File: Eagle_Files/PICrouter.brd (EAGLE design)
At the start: 101.8 x 34 mm, 81 parts, among them IC1 PIC32MX675F512H, IC2 48M033F, IC3 DP83848, J3 POWER_JACK, Q1 20MHz, U1 DEVICE, X1 USB-A-H

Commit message: Released PICrouter schematic and board v0.91.
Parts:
- removed C25: 150uF, rcl:PANASONIC_C
- removed C27: 0.1uF, rcl:C2012
- removed D1, D2: (no value), diode:SOD123
- removed F1: PTCSMD, SparkFun:PTC-1206
- removed J3: POWER_JACK, SparkFun:POWER_JACK_PTH_LOCK
- removed Q2: (no value), transistor-small-signal:SOT23
- removed R7: 33k, SparkFun:0603-RES
- removed U1: DEVICE, SparkFun:USB-B-PTH
- removed X1: USB-A-H, SparkFun:USB-A-H
- added C28, C29, C31, C32: 0.1uF, rcl:C2012
- added C30: 10uF, rcl:C2012
- added F2: PTCSMD, SparkFun:PTC-1206
- added IC4: TPS2111A, SparkFun:TSSOP8
- added J1: POWER_JACK, SparkFun:POWER_JACK_PTH_LOCK
- added R28: 400, SparkFun:0603-RES
- added U2: DEVICE, SparkFun:USB-B-PTH
- added X2: USB-A-H, SparkFun:USB-A-H
- C10: value 0.1uF -> 150uF; device rcl:C2012 -> rcl:PANASONIC_C
- C13: value 10uF -> 150uF; device rcl:C2012 -> rcl:PANASONIC_C
- R6: value 100k -> 10k
- moved C13 21.2 mm to (-9.02, 3.81), turned to 0 degrees
- moved R5 13.2 mm to (31.2, 6.81), turned to 180 degrees
- moved C10 5.41 mm to (12.2, 8.89)
- moved R6 1.18 mm to (21.8, 11.7), turned to 270 degrees
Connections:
- removed net N$45: IC1.36, U1.D-, X1.D-
- removed net N$46: C10.1, C27.1, D1.A, J3.PWR, PW.1, Q2.1, R5.2, R7.2
- removed net N$5: IC1.37, U1.D+, X1.D+
- removed net N$50: C13.1, C25.+, C9.2, F1.1, IC1.34, Q2.2, R4.1, R6.2, U1.VBUS, X1.VBUS
- removed net N$60: D2.A, Q2.3
- new net D+: IC1.37, U2.D+, X2.D+
- new net D-: IC1.36, U2.D-, X2.D-
- new net N$61: IC4.4, R28.2
- new net SELF: C29.1, C31.1, C32.1, IC4.2, IC4.8, J1.PWR, PW.1, R5.2, R6.2
- new net VBUS: C28.1, C30.1, C9.2, IC1.34, IC4.6, R4.1, U2.VBUS
- new net VBUS_HOST: C10.+, F2.2, X2.VBUS
- net GND: now also C10.-, C13.-, C28.2, C29.2, C30.2, C31.2, C32.2, IC4.1, IC4.3, IC4.5, J1.GND, R28.1, U2.GND, U2.S1, U2.S2, X2.GND, X2.GND2, X2.GND3; no longer C10.2, C13.2, C25.-, C27.2, J3.GND, R7.1, U1.GND, U1.S1, U1.S2, X1.GND, X1.GND2, X1.GND3
- net VCC: now also C13.+, F2.1, IC4.7; no longer D1.C, D2.C, F1.2
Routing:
- net N$50: track 111.3 -> 0.00 mm, vias 4 -> 0
- net SELF: track 0.00 -> 106.7 mm, vias 0 -> 5
- net N$46: track 102.3 -> 0.00 mm, vias 2 -> 0
- net VBUS: track 0.00 -> 76.6 mm, vias 0 -> 4
- net D+: track 0.00 -> 68.6 mm, vias 0 -> 1
- net D-: track 0.00 -> 66.1 mm, vias 0 -> 2
- net N$45: track 66.3 -> 3.45 mm, vias 1 -> 0
- net N$5: track 68.0 -> 12.8 mm, vias 1 -> 0
- net N$11: track 37.6 -> 14.3 mm, vias 2 -> 0
- net VBUS_HOST: track 0.00 -> 17.5 mm
- net GND: track 204.2 -> 218.0 mm, vias 29 -> 48
- net N$44: track 0.00 -> 9.78 mm
- net VCC: track 28.7 -> 34.2 mm, vias 2 -> 0
- net N$60: track 1.93 -> 0.00 mm
- net N$61: track 0.00 -> 1.41 mm
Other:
- board size 101.8 x 34 mm -> 100 x 34 mm
- board text added: "Bridge between OSC and USB_MIDI"
- board text added: "v0.91/CC by-SA 3.0"
- board text removed: "/* Bridge between OSC and USB_MIDI */"
- board text removed: "v0.9/CC by-SA 3.0"

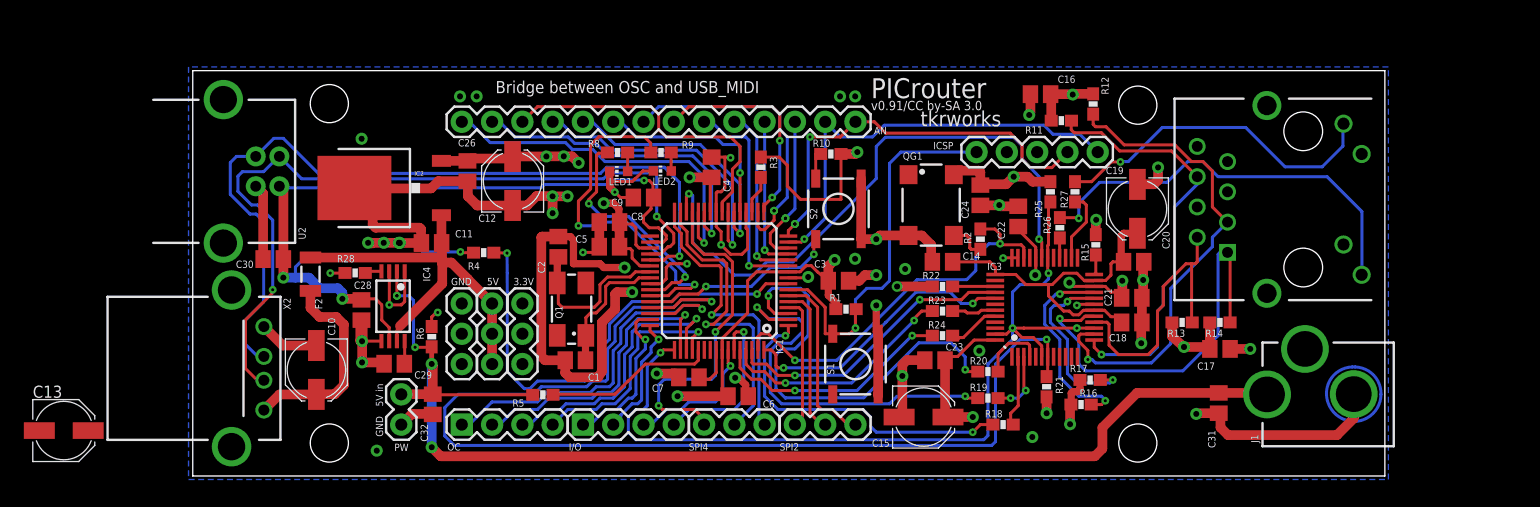
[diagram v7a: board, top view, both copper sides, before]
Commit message: Released PICrouter schematic and board v0.92.
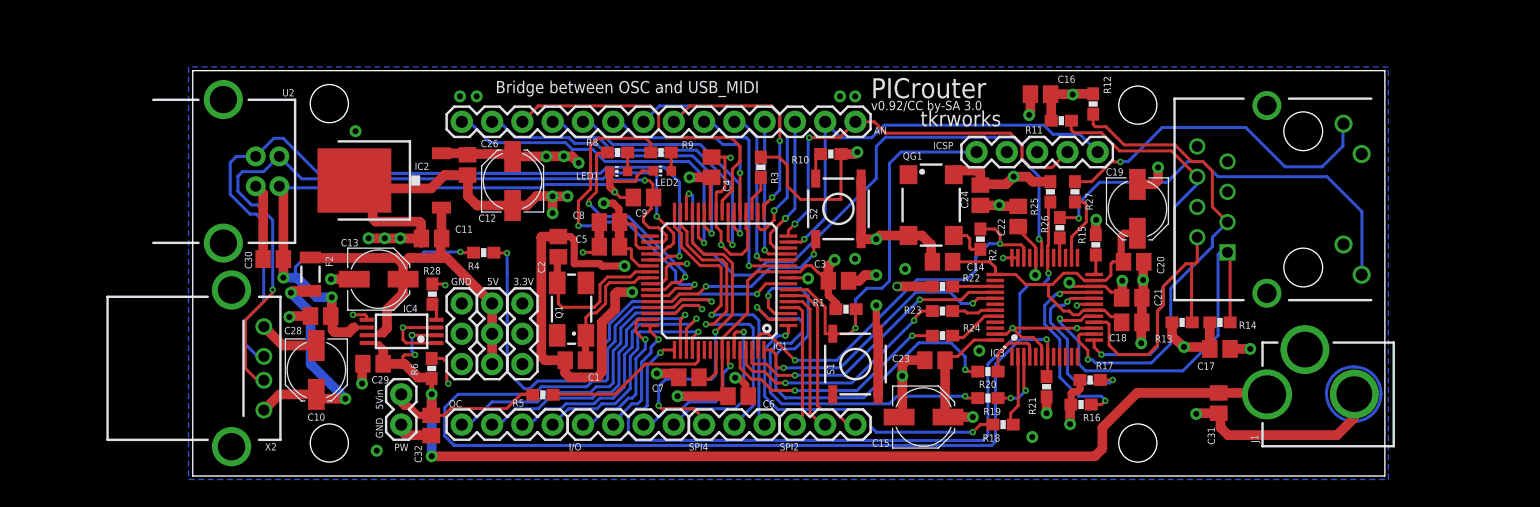
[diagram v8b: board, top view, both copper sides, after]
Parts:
- C13: value 150uF -> 100uF
- moved C13 29.3 mm to (17.4, 16.5)
- moved R28 6.72 mm to (21.9, 15.3), turned to 270 degrees
- moved C28 3.47 mm to (12.5, 13.4), turned to 180 degrees
- moved R6 2.67 mm to (21.8, 9.02)
- moved IC4 2.23 mm to (19.3, 12.1), turned to 180 degrees
- moved C32 1.78 mm to (21.8, 4.23)
- moved C29 1.78 mm to (16.9, 9.42)
- moved IC2 0.64 mm to (17.9, 24.8)
- moved C26 0.51 mm to (24.8, 26.1)
- moved C11 0.38 mm to (21.8, 19.9)
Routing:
- net GND: track 218.0 -> 220.9 mm, vias 48 -> 49
- net VBUS_HOST: track 17.5 -> 20.0 mm, vias 0 -> 2
- net VBUS: track 76.6 -> 74.4 mm
- net N$64: track 0.00 -> 1.93 mm
- net N$66: track 0.00 -> 1.58 mm
- net N$50: track 0.00 -> 1.37 mm
- net N$51: track 0.00 -> 1.10 mm
- net N$63: track 0.00 -> 1.03 mm
- net SELF: track 106.7 -> 107.6 mm
- net N$60: track 0.00 -> 0.82 mm
- net N$59: track 0.00 -> 0.61 mm
- net N$46: track 0.00 -> 0.55 mm
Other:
- board text added: "5Vin"
- board text added: "v0.92/CC by-SA 3.0"
- board text removed: "5V in"
- board text removed: "v0.91/CC by-SA 3.0"
